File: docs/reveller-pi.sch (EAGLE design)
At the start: 17 parts, among them Q1 BS270, X1 CANTON-POWER, X2 RASPI_BOARD_AB_E0, X3 PG203J

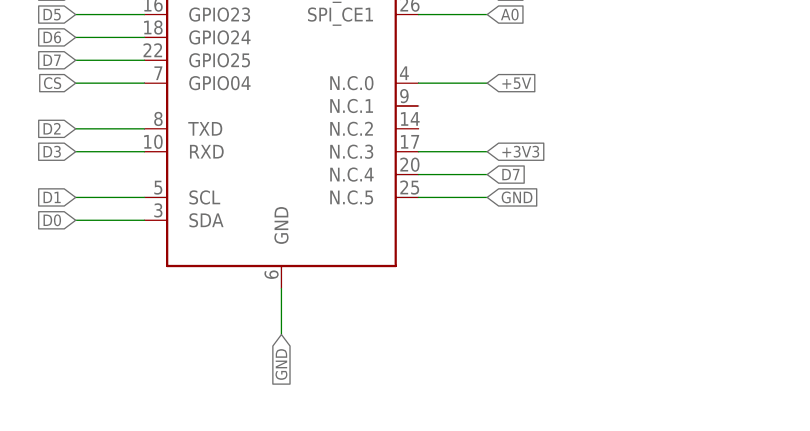
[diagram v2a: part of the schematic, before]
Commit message: removed mistaken D7 connection to pin 20, switched rpi header gnd to gnd-symbol, switched capacitors to 2.5x5
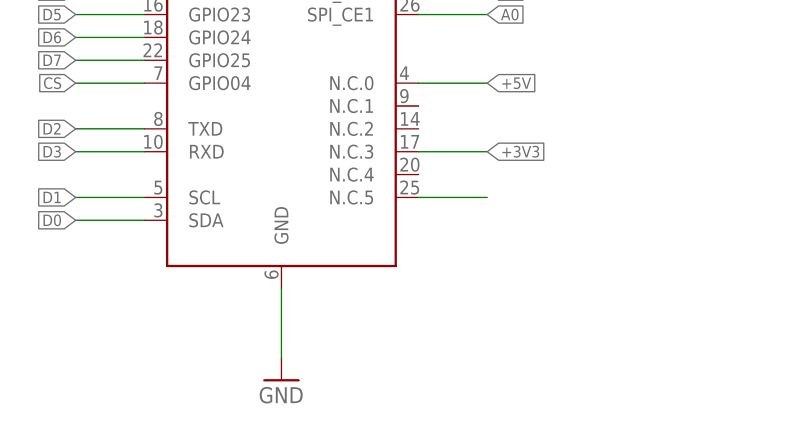
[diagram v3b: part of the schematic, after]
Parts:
- C4, C5, C6, C7, C8: device rcl:CPOL-EUE15-5AXIAL -> rcl:CPOL-EUE2.5-5
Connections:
- net D7: no longer X2.N.C.4
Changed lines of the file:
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@@
 <part name="R2" library="rcl" deviceset="R-EU_" device="0204/7" value="3.3k"/>
 <part name="+3V1" library="supply1" deviceset="+3V3" device=""/>
-<part name="C4" library="rcl" deviceset="CPOL-EU" device="E15-5AXIAL" value="1nF"/>
+<part name="C4" library="rcl" deviceset="CPOL-EU" device="E2.5-5" value="1nF"/>
 <part name="GND2" library="supply1" deviceset="GND" device=""/>
 <part name="R1" library="rcl" deviceset="R-EU_" device="0204/7" value="1k"/>
 <part name="GND3" library="supply1" deviceset="GND" device=""/>
-<part name="C5" library="rcl" deviceset="CPOL-EU" device="E15-5AXIAL" value="0.1uF"/>
-<part name="C6" library="rcl" deviceset="CPOL-EU" device="E15-5AXIAL" value="10uF"/>
-<part name="C7" library="rcl" deviceset="CPOL-EU" device="E15-5AXIAL" value="0.1uF"/>
-<part name="C8" library="rcl" deviceset="CPOL-EU" device="E15-5AXIAL" value="10uF"/>
+<part name="C5" library="rcl" deviceset="CPOL-EU" device="E2.5-5" value="0.1uF"/>
+<part name="C6" library="rcl" deviceset="CPOL-EU" device="E2.5-5" value="10uF"/>
+<part name="C7" library="rcl" deviceset="CPOL-EU" device="E2.5-5" value="0.1uF"/>
+<part name="C8" library="rcl" deviceset="CPOL-EU" device="E2.5-5" value="10uF"/>
 <part name="GND4" library="supply1" deviceset="GND" device=""/>
 <part name="X2" library="raspberrypi_bastelstube_v13" deviceset="RASPI_BOARD_AB" device="_E0"/>
@@
 <part name="X3" library="con-hirschmann" deviceset="PG203J" device=""/>
 <part name="GND5" library="supply1" deviceset="GND" device=""/>
+<part name="GND6" library="supply1" deviceset="GND" device=""/>
 </parts>
 <sheets>
@@
 <instance part="X3" gate="1" x="231.14" y="96.52"/>
 <instance part="GND5" gate="1" x="218.44" y="55.88"/>
+<instance part="GND6" gate="1" x="53.34" y="35.56"/>
 </instances>
 <busses>
@@
 <pinref part="X2" gate="G$1" pin="N.C.5"/>
 <wire x1="68.58" y1="55.88" x2="76.2" y2="55.88" width="0.1524" layer="91"/>
-<label x="76.2" y="55.88" size="1.27" layer="95" xref="yes"/>
 </segment>
 <segment>
@@
 </segment>
 <segment>
+<pinref part="GND6" gate="1" pin="GND"/>
 <pinref part="X2" gate="G$1" pin="GND"/>
-<wire x1="53.34" y1="45.72" x2="53.34" y2="40.64" width="0.1524" layer="91"/>
-<label x="53.34" y="40.64" size="1.27" layer="95" rot="R270" xref="yes"/>
+<wire x1="53.34" y1="38.1" x2="53.34" y2="45.72" width="0.1524" layer="91"/>
 </segment>
 </net>
@@
 </segment>
 <segment>
-<pinref part="X2" gate="G$1" pin="N.C.4"/>
-<wire x1="68.58" y1="58.42" x2="76.2" y2="58.42" width="0.1524" layer="91"/>
-<label x="76.2" y="58.42" size="1.27" layer="95" xref="yes"/>
-</segment>
-<segment>

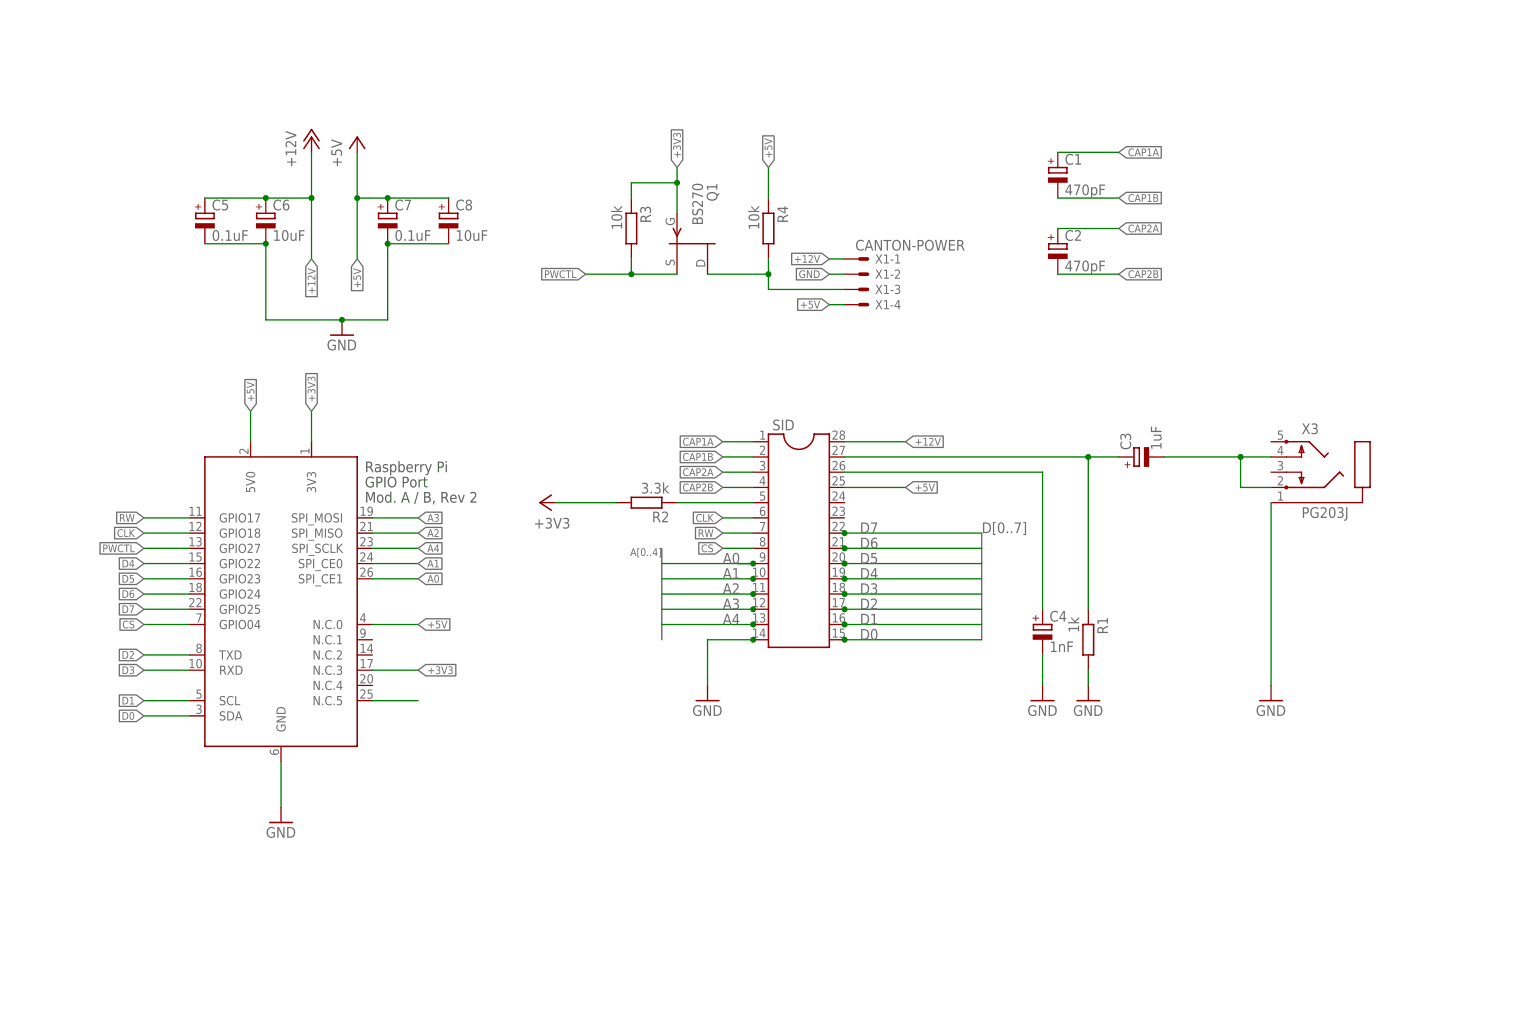
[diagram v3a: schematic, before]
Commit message: Added boarddesign
Added boarddesign and some revisions on the schmatic regarding safety
features for the SID Chip
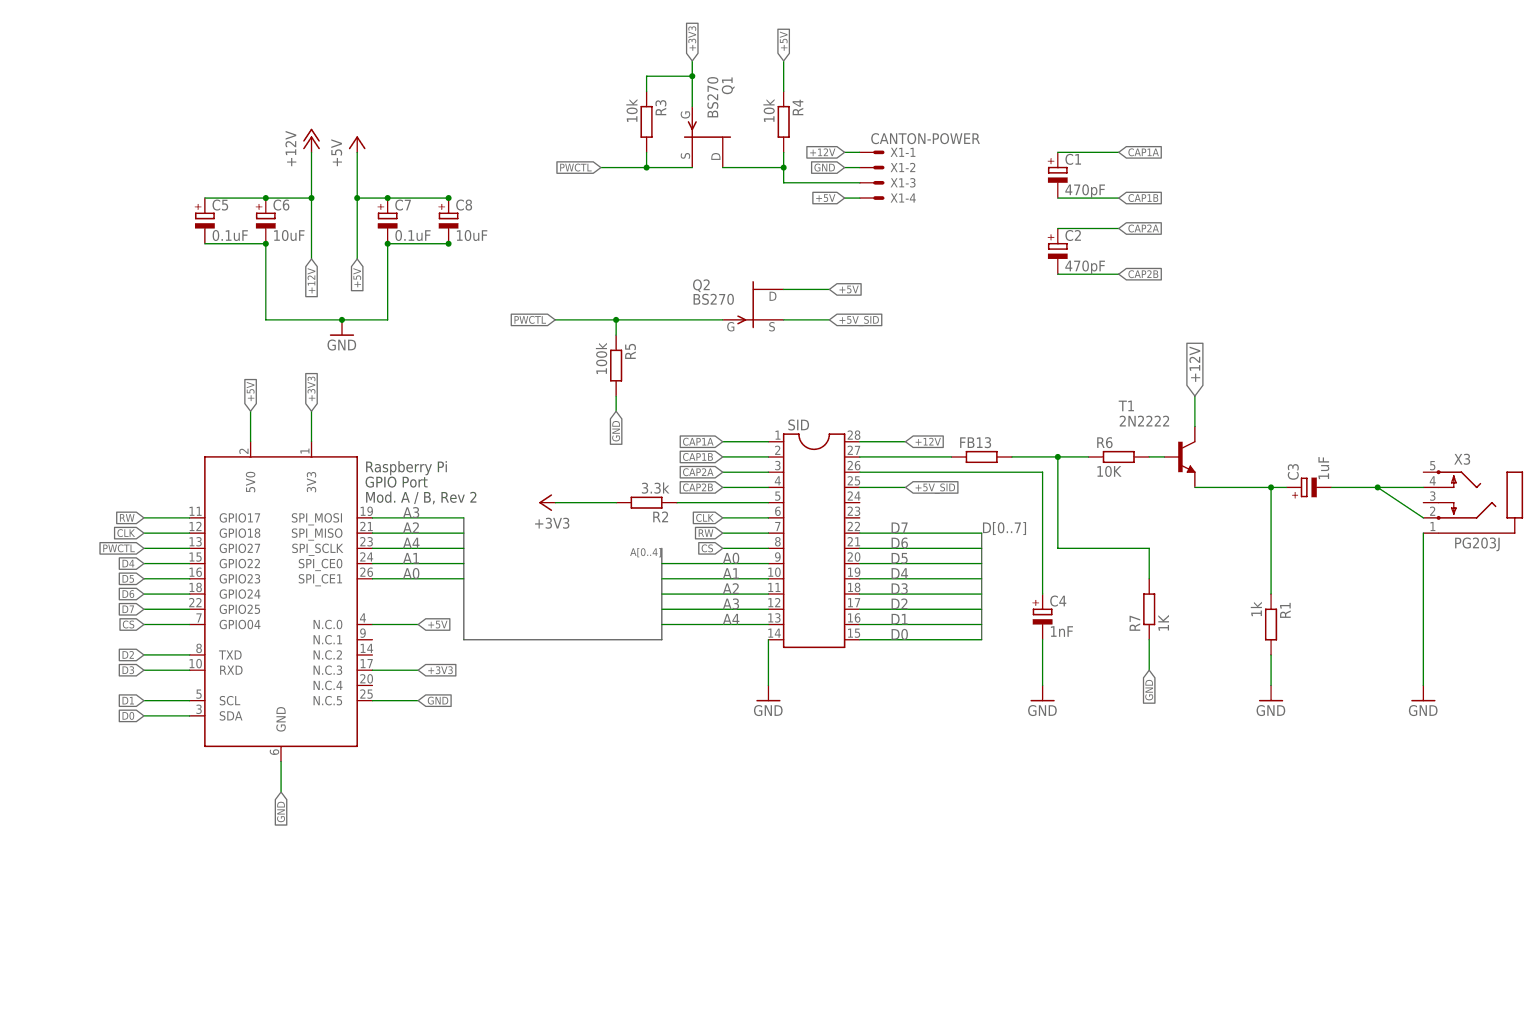
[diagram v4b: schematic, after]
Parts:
- added FB13: (no value), rcl:R-EU_0204/7
- added Q2: BS270, transistor-fet:2N5484
- added R5: 100k, rcl:R-EU_0204/7
- added R6: 10K, rcl:R-EU_0204/7
- added R7: 1K, rcl:R-EU_0204/7
- added T1: 2N2222, transistor:2N2222
- C1, C2, C3: device rcl:CPOL-EUE2-4 -> rcl:CPOL-EUE2.5-5
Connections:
- new net +5V_SID: Q2.S, SID.25
- new net N$5: R6.2, T1.B
- new net N$6: FB13.1, SID.27
- new net N$7: R5.2
- new net N$8: FB13.2, R6.1, R7.2
- net +12V: now also T1.C
- net +5V: now also Q2.D; no longer SID.25
- net GND: now also R7.1
- net N$2: now also T1.E; no longer SID.27
- net PWCTL: now also Q2.G, R5.1
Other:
- moved on the sheet: C3, C4, Q1, R1, R3, R4, SID, X1-1, X1-2, X1-3, X1-4, X3

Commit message: Revised boarddesign and schmatic for better powercontrol
Cleaned up the board with, everything done by Morten Leikvoll.
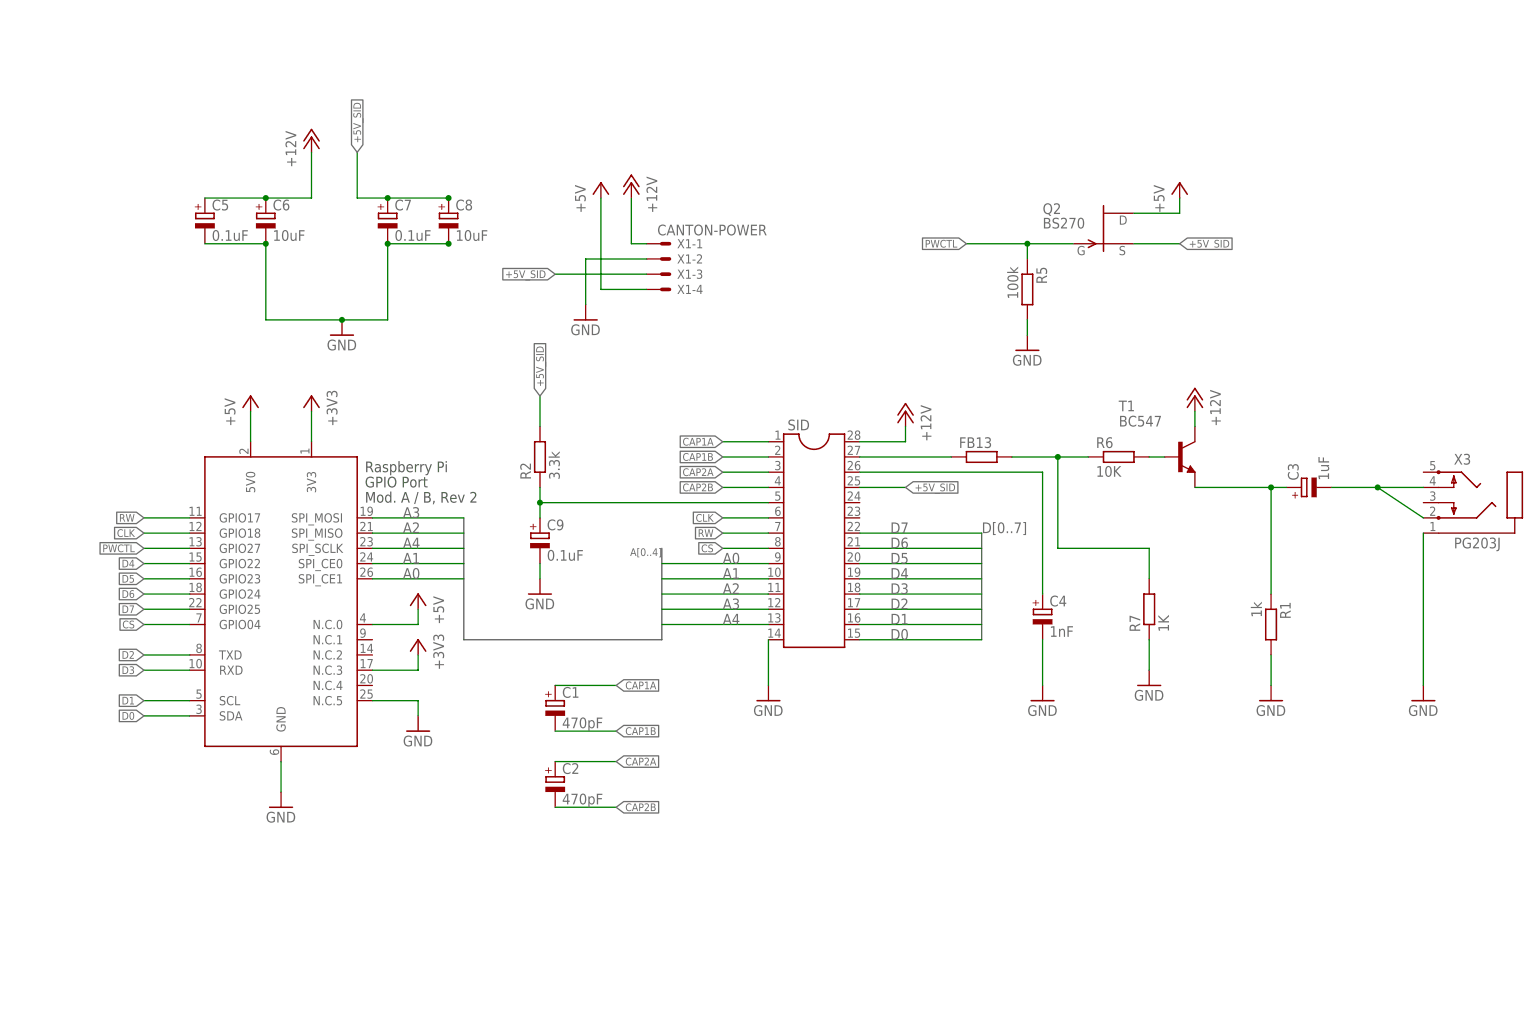
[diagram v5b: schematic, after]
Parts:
- removed Q1: BS270, transistor-fet:2N5484
- removed R3, R4: 10k, rcl:R-EU_0204/7
- added C9: 0.1uF, rcl:CPOL-EUE2.5-5
- T1: value 2N2222 -> BC547; device transistor:2N2222 -> transistor:BC547
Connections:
- net N$1 renamed CAPX
- net N$2 renamed AUDIO_DC
- net N$3 renamed AUDIO_OUT
- net N$5 renamed AUDIO_PREAMP_B
- net N$6 renamed AUDIO_RAW
- net N$8 renamed AUDIO_PREAMP
- removed net N$4: Q1.D, R4.2, X1-3.S
- removed net N$7: R5.2
- net +3V3: no longer Q1.G, R2.2, R3.1
- net +5V: no longer C7.+, C8.+, R4.1
- net +5V_SID: now also C7.+, C8.+, R2.2, X1-3.S
- net GND: now also C9.-, R5.2
- net PWCTL: no longer Q1.S, R3.2
- net RESET: now also C9.+
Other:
- moved on the sheet: C1, C2, Q2, R2, R5, X1-1, X1-2, X1-3, X1-4

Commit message: More revisions...
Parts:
- FB13: value (none) -> 0R
- SID: value (none) -> 6581
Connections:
- removed net +3V3: X2.3V3, X2.N.C.3
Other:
- note added: "Reveller Sid Player #FluXxX"
- note added: "V0.1"
- moved on the sheet: C1, C2, C3, C4, C5, C6, C7, C8, C9, FB13, Q2, R1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

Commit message: Completed powercontrol and boarddesign
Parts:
- removed C1, C2: 470pF, rcl:CPOL-EUE2.5-5
- removed C3: 1uF, rcl:CPOL-EUE2.5-5
- removed C4: 1nF, rcl:CPOL-EUE2.5-5
- removed C5, C7, C9: 0.1uF, rcl:CPOL-EUE2.5-5
- removed C6, C8: 10uF, rcl:CPOL-EUE2.5-5
- removed FB13: 0R, rcl:R-EU_0204/7
- removed Q2: BS270, transistor-fet:2N5484
- removed R1: 1k, rcl:R-EU_0204/7
- removed R2: 3.3k, rcl:R-EU_0204/7
- removed R5: 100k, rcl:R-EU_0204/7
- removed R6: 10K, rcl:R-EU_0204/7
- removed R7: 1K, rcl:R-EU_0204/7
- removed SID: 6581, ic-package:DIL28
- removed T1: BC547, transistor:BC547
- removed X1: CANTON-POWER, con-molex:22-23-2041
- removed X2: RASPI_BOARD_AB_E0, raspberrypi_bastelstube_v13:RASPI_BOARD_AB_E0
- removed X3: PG203J, con-hirschmann:PG203J
- added C100, C105, C107: 0.1uF, rcl:CPOL-EUE2.5-5
- added C101: 1nF, rcl:CPOL-EUE2.5-5
- added C102: 1uF, rcl:CPOL-EUE2.5-5
- added C103, C104: 470pF, rcl:CPOL-EUE2.5-5
- added C106, C108: 10uF, rcl:CPOL-EUE2.5-5
- added IC100: 6581, ic-package:DIL28
- added Q100: IRF9Z24N, transistor-power:IRF9530
- added R100: 1K, rcl:R-EU_0204/7
- added R101: 1k, rcl:R-EU_0204/7
- added R102: 3.3k, rcl:R-EU_0204/7
- added R103: 0R, rcl:R-EU_0204/7
- added R104: 10K, rcl:R-EU_0204/7
- added R105: NM*, rcl:R-EU_0204/7
- added T100: BC547, transistor:BC547
- added X100: RASPI_BOARD_AB_E0, raspberrypi_bastelstube_v13:RASPI_BOARD_AB_E0
- added X101: PG203J, con-hirschmann:PG203J
- added X102: CANTON-POWER, con-molex:22-23-2041
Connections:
- net +12V: now also C105.+, C106.+, IC100.28, T100.C, X102-1.S; no longer C5.+, C6.+, SID.28, T1.C, X1-1.S
- net +5V: now also Q100.S, R105.2, X100.5V0, X100.N.C.0, X102-4.S; no longer Q2.D, X1-4.S, X2.5V0, X2.N.C.0
- net +5V_SID: now also C107.+, C108.+, IC100.25, Q100.D, R102.2; no longer C7.+, C8.+, Q2.S, R2.2, SID.25, X1-3.S
- net A0: now also IC100.9, X100.SPI_CE1; no longer SID.9, X2.SPI_CE1
- net A1: now also IC100.10, X100.SPI_CE0; no longer SID.10, X2.SPI_CE0
- net A2: now also IC100.11, X100.SPI_MISO; no longer SID.11, X2.SPI_MISO
- net A3: now also IC100.12, X100.SPI_MOSI; no longer SID.12, X2.SPI_MOSI
- net A4: now also IC100.13, X100.SPI_SCLK; no longer SID.13, X2.SPI_SCLK
- net AUDIO_DC: now also C102.+, R101.1, T100.E; no longer C3.+, R1.1, T1.E
- net AUDIO_OUT: now also C102.-, X101.2, X101.4; no longer C3.-, X3.2, X3.4
- net AUDIO_PREAMP: now also R100.2, R103.2, R104.1; no longer FB13.2, R6.1, R7.2
- net AUDIO_PREAMP_B: now also R104.2, T100.B; no longer R6.2, T1.B
- net AUDIO_RAW: now also IC100.27, R103.1; no longer FB13.1, SID.27
- net CAP1A: now also C104.+, IC100.1; no longer C1.+, SID.1
- net CAP1B: now also C104.-, IC100.2; no longer C1.-, SID.2
- net CAP2A: now also C103.+, IC100.3; no longer C2.+, SID.3
- net CAP2B: now also C103.-, IC100.4; no longer C2.-, SID.4
- net CAPX: now also C101.+, IC100.26; no longer C4.+, SID.26
- net CLK: now also IC100.6, X100.GPIO18; no longer SID.6, X2.GPIO18
- net CS: now also IC100.8, X100.GPIO04; no longer SID.8, X2.GPIO04
- net D0: now also IC100.15, X100.SDA; no longer SID.15, X2.SDA
- net D1: now also IC100.16, X100.SCL; no longer SID.16, X2.SCL
- net D2: now also IC100.17, X100.TXD; no longer SID.17, X2.TXD
- net D3: now also IC100.18, X100.RXD; no longer SID.18, X2.RXD
- net D4: now also IC100.19, X100.GPIO22; no longer SID.19, X2.GPIO22
- net D5: now also IC100.20, X100.GPIO23; no longer SID.20, X2.GPIO23
- net D6: now also IC100.21, X100.GPIO24; no longer SID.21, X2.GPIO24
- net D7: now also IC100.22, X100.GPIO25; no longer SID.22, X2.GPIO25
- net GND: now also C100.-, C101.-, C105.-, C106.-, C107.-, C108.-, IC100.14, R100.1, R101.2, X100.GND, X100.N.C.5, X101.1, X102-2.S; no longer C4.-, C5.-, C6.-, C7.-, C8.-, C9.-, R1.2, R5.2, R7.1, SID.14, X1-2.S, X2.GND, X2.N.C.5, X3.1
- net PWCTL: now also Q100.G, R105.1, X100.GPIO27, X102-3.S; no longer Q2.G, R5.1, X2.GPIO27
- net RESET: now also C100.+, IC100.5, R102.1; no longer C9.+, R2.1, SID.5
- net RW: now also IC100.7, X100.GPIO17; no longer SID.7, X2.GPIO17
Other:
- note added: "* R105 is present inside the canton power module, so no need for it here"
- note added: "PWCTL: low=on high/open=off"
